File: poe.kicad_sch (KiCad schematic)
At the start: 5 parts, among them J4 Connector_RJ45_Magjack_Abraco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, J5 Connector_RJ45_Magjack_Abraco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, U8 TVS3300DRV

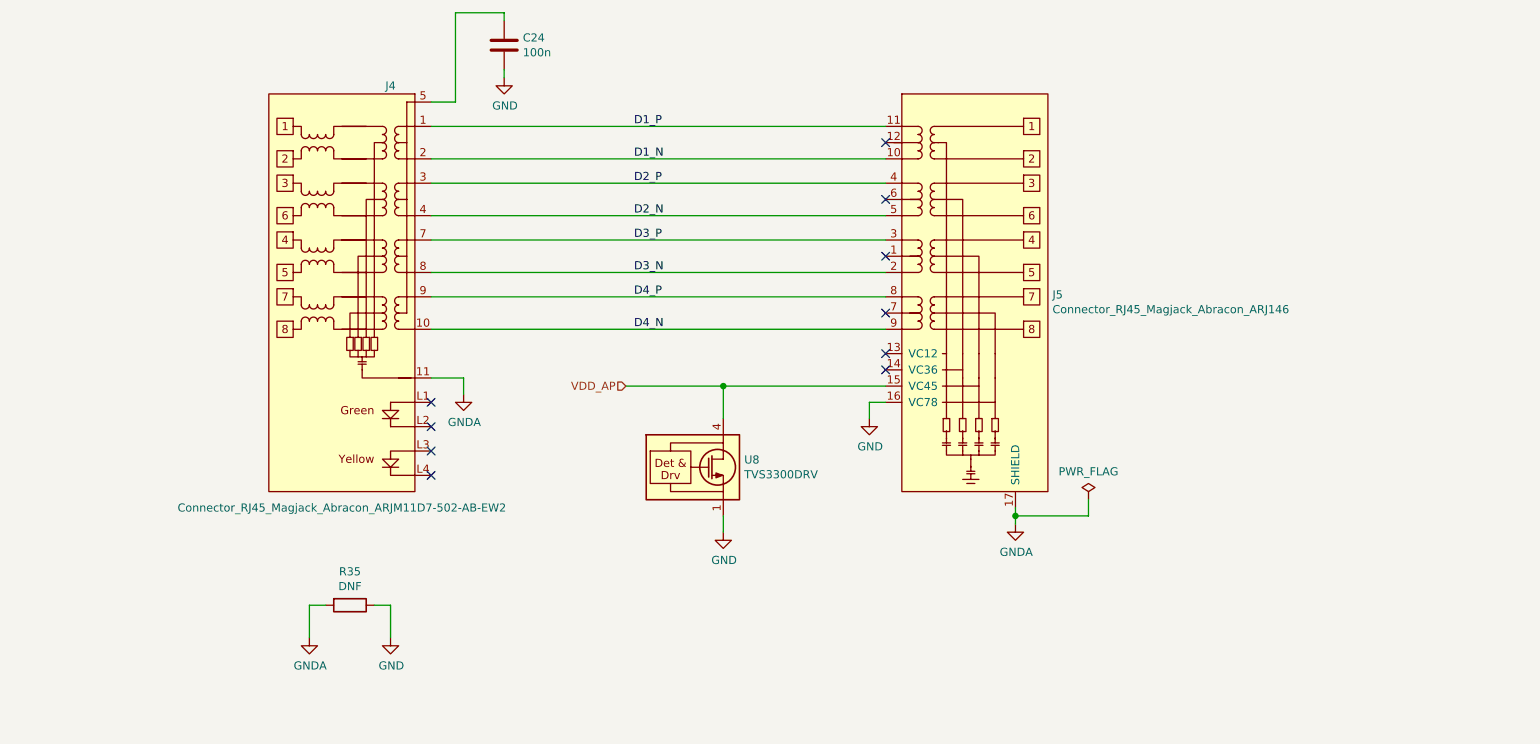
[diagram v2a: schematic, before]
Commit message: Started new connector layout
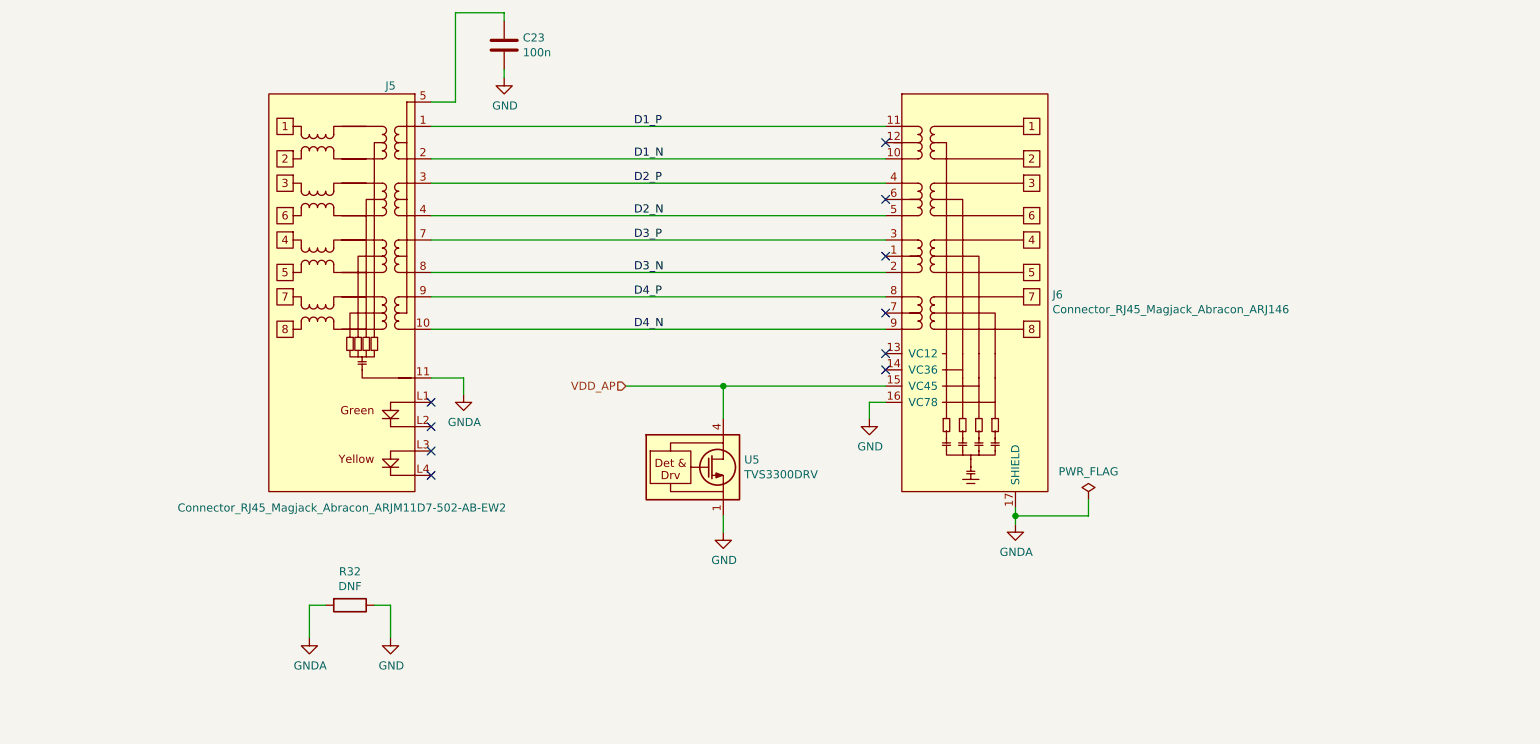
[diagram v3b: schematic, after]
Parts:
- renumbered C24 to C23, J4 to J5, J5 to J6, R35 to R32, U8 to U5
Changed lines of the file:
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@@
   (junction (at 138.43 119.38) (diameter 1.016) (color 0 0 0 0))
   (junction (at 184.15 139.7) (diameter 1.016) (color 0 0 0 0))
-  (no_connect (at 163.83 114.3))
+  (no_connect (at 92.71 121.92))
+  (no_connect (at 92.71 125.73))
+  (no_connect (at 92.71 129.54))
+  (no_connect (at 92.71 133.35))
+  (no_connect (at 163.83 81.28))
+  (no_connect (at 163.83 90.17))
   (no_connect (at 163.83 99.06))
   (no_connect (at 163.83 107.95))
-  (no_connect (at 92.71 125.73))
+  (no_connect (at 163.83 114.3))
   (no_connect (at 163.83 116.84))
-  (no_connect (at 92.71 129.54))
-  (no_connect (at 92.71 133.35))
-  (no_connect (at 163.83 90.17))
-  (no_connect (at 92.71 121.92))
-  (no_connect (at 163.83 81.28))
   (wire (pts (xy 73.66 153.67) (xy 73.66 158.75))
     (stroke (width 0) (type solid) (color 0 0 0 0))
@@
   (symbol (lib_id "power:GNDA") (at 73.66 158.75 0) (unit 1)
     (in_bom yes) (on_board yes)
-    (property "Reference" "#PWR070" (id 0) (at 73.66 165.1 0)
+    (property "Reference" "#PWR060" (id 0) (at 73.66 165.1 0)
       (effects (font (size 1.27 1.27)) hide)
     )
@@
   (symbol (lib_id "power:GND") (at 86.36 158.75 0) (unit 1)
     (in_bom yes) (on_board yes)
-    (property "Reference" "#PWR071" (id 0) (at 86.36 165.1 0)
+    (property "Reference" "#PWR061" (id 0) (at 86.36 165.1 0)
       (effects (font (size 1.27 1.27)) hide)
     )
@@
   (symbol (lib_id "power:GNDA") (at 97.79 120.65 0) (unit 1)
     (in_bom yes) (on_board yes)
-    (property "Reference" "#PWR067" (id 0) (at 97.79 127 0)
+    (property "Reference" "#PWR056" (id 0) (at 97.79 127 0)
       (effects (font (size 1.27 1.27)) hide)
     )
@@
   (symbol (lib_id "power:GND") (at 104.14 71.12 0) (unit 1)
     (in_bom yes) (on_board yes)
-    (property "Reference" "#PWR066" (id 0) (at 104.14 77.47 0)
+    (property "Reference" "#PWR055" (id 0) (at 104.14 77.47 0)
       (effects (font (size 1.27 1.27)) hide)
     )
@@
   (symbol (lib_id "power:GND") (at 138.43 142.24 0) (unit 1)
     (in_bom yes) (on_board yes)
-    (property "Reference" "#PWR0101" (id 0) (at 138.43 148.59 0)
+    (property "Reference" "#PWR059" (id 0) (at 138.43 148.59 0)
       (effects (font (size 1.27 1.27)) hide)
     )
@@
   (symbol (lib_id "power:GND") (at 161.29 124.46 0) (unit 1)
     (in_bom yes) (on_board yes)
-    (property "Reference" "#PWR068" (id 0) (at 161.29 130.81 0)
+    (property "Reference" "#PWR057" (id 0) (at 161.29 130.81 0)
       (effects (font (size 1.27 1.27)) hide)
     )
@@
   (symbol (lib_id "power:GNDA") (at 184.15 140.97 0) (unit 1)
     (in_bom yes) (on_board yes)
-    (property "Reference" "#PWR069" (id 0) (at 184.15 147.32 0)
+    (property "Reference" "#PWR058" (id 0) (at 184.15 147.32 0)
       (effects (font (size 1.27 1.27)) hide)
     )
@@
   (symbol (lib_id "Device:R") (at 80.01 153.67 270) (unit 1)
     (in_bom yes) (on_board yes)
-    (property "Reference" "R35" (id 0) (at 80.01 148.4122 90))
+    (property "Reference" "R32" (id 0) (at 80.01 148.4122 90))
     (property "Value" "DNF" (id 1) (at 80.01 150.7236 90))
     (property "Footprint" "Resistor_SMD:R_0805_2012Metric" (id 2) (at 80.01 151.892 90)
@@
   (symbol (lib_id "Device:C") (at 104.14 66.04 0) (unit 1)
     (in_bom yes) (on_board yes)
-    (property "Reference" "C24" (id 0) (at 107.061 64.8716 0)
+    (property "Reference" "C23" (id 0) (at 107.061 64.8716 0)
       (effects (font (size 1.27 1.27)) (justify left))
     )
@@
   (symbol (lib_id "Power_Protection:TVS3300DRV") (at 138.43 132.08 0) (unit 1)
     (in_bom yes) (on_board yes)
-    (property "Reference" "U8" (id 0) (at 141.7066 130.9116 0)
+    (property "Reference" "U5" (id 0) (at 141.7066 130.9116 0)
       (effects (font (size 1.27 1.27)) (justify left))
     )
@@
   (symbol (lib_id "Connector_WUT:Connector_RJ45_Magjack_Abracon_ARJM11D7-502-AB-EW2") (at 78.74 91.44 0) (mirror y) (unit 1)
     (in_bom yes) (on_board yes)
-    (property "Reference" "J4" (id 0) (at 86.36 72.39 0))
+    (property "Reference" "J5" (id 0) (at 86.36 72.39 0))
     (property "Value" "Connector_RJ45_Magjack_Abracon_ARJM11D7-502-AB-EW2" (id 1) (at 78.74 138.43 0))
     (property "Footprint" "Connector_WUT:Connector_RJ45_Magjack_Abracon_ARJM11D7-502-AB-EW2" (id 2) (at 86.36 91.44 0)
@@
   (symbol (lib_id "Connector_WUT:Connector_RJ45_Magjack_Abracon_ARJ146") (at 177.8 91.44 0) (unit 1)
     (in_bom yes) (on_board yes)
-    (property "Reference" "J5" (id 0) (at 189.9412 105.0798 0)
-      (effects (font (size 1.27 1.27)) (justify left))
-    )
+    (property "Reference" "J6" (id 0) (at 189.9412 105.0798 0)
+      (effects (font (size 1.27 1.27)) (justify left))
+    )

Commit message: Mostly complete, just missing a few tracks and review
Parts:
- removed J5: Connector_RJ45_Magjack_Abracon_ARJM11D7-502-AB-EW2, Connector_WUT:Connector_RJ45_Magjack_Abracon_ARJM11D7-502-AB-EW2, symbol Connector_WUT:Connector_RJ45_Magjack_Abracon_ARJM11D7-502-AB-EW2
- removed R32: DNF, Resistor_SMD:R_0805_2012Metric, symbol Device:R
- removed U5: TVS3300DRV, Package_SON:WSON-6-1EP_2x2mm_P0.65mm_EP1x1.6mm, symbol Power_Protection:TVS3300DRV
- added C24: 47u, Capacitor_SMD:C_1206_3216Metric, symbol Device:C
- added C25, C26, C27, C28: 100n, Capacitor_SMD:C_0603_1608Metric, symbol Device:C
- added D1: P6SMB36CA-Q, Diode_SMD:D_SMB, symbol Device:D_TVS
- added J5: Connector_RJ45_Magjack_Abracon_ARJM11D7-502-NN-EW2, Connector_WUT:Connector_RJ45_Magjack_Abracon_ARJM11D7-502-NN-EW2, symbol Connector_WUT:Connector_RJ45_Magjack_Abracon_ARJM11D7-502-NN-EW2
- added R37: DNF, Resistor_SMD:R_0603_1608Metric, symbol Device:R
- C23: footprint Capacitor_SMD:C_0402_1005Metric -> Capacitor_SMD:C_0603_1608Metric
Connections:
- net D1_N: now also J5.2
- net D1_P: now also J5.1
- net D2_N: now also J5.4
- net D2_P: now also J5.3
- net D3_N: now also J5.8
- net D3_P: now also J5.7
- net D4_N: now also J5.10
- net D4_P: now also J5.9
- net GND: now also C24.2, C25.2, C26.2, C27.2, C28.2, D1.1 (A1), R37.1
- net GNDA: now also J5.11, R37.2
- net VDD_AP: now also C24.1, D1.2 (A2)
- net at J6.1: now also C27.1
- net at J6.12: now also C25.1
- net at J6.6: now also C26.1
- net at J6.7: now also C28.1
- net at C23.1: now also J5.5, J5.6
- no-connect marks 10 -> 2
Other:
- moved on the sheet: J6
